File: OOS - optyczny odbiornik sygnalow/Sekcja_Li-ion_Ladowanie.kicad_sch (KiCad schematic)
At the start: 41 parts, among them J1 Conn_01x02_Pin, Q1 SI2301CDS-T1-GE3, Q2 AOSS32334C, Q3 AOSS32334C, U4 MCP73831-2-OT, U5 AP9101CAK6-ANTRG1, U6 AP2126K-ADJTRG1

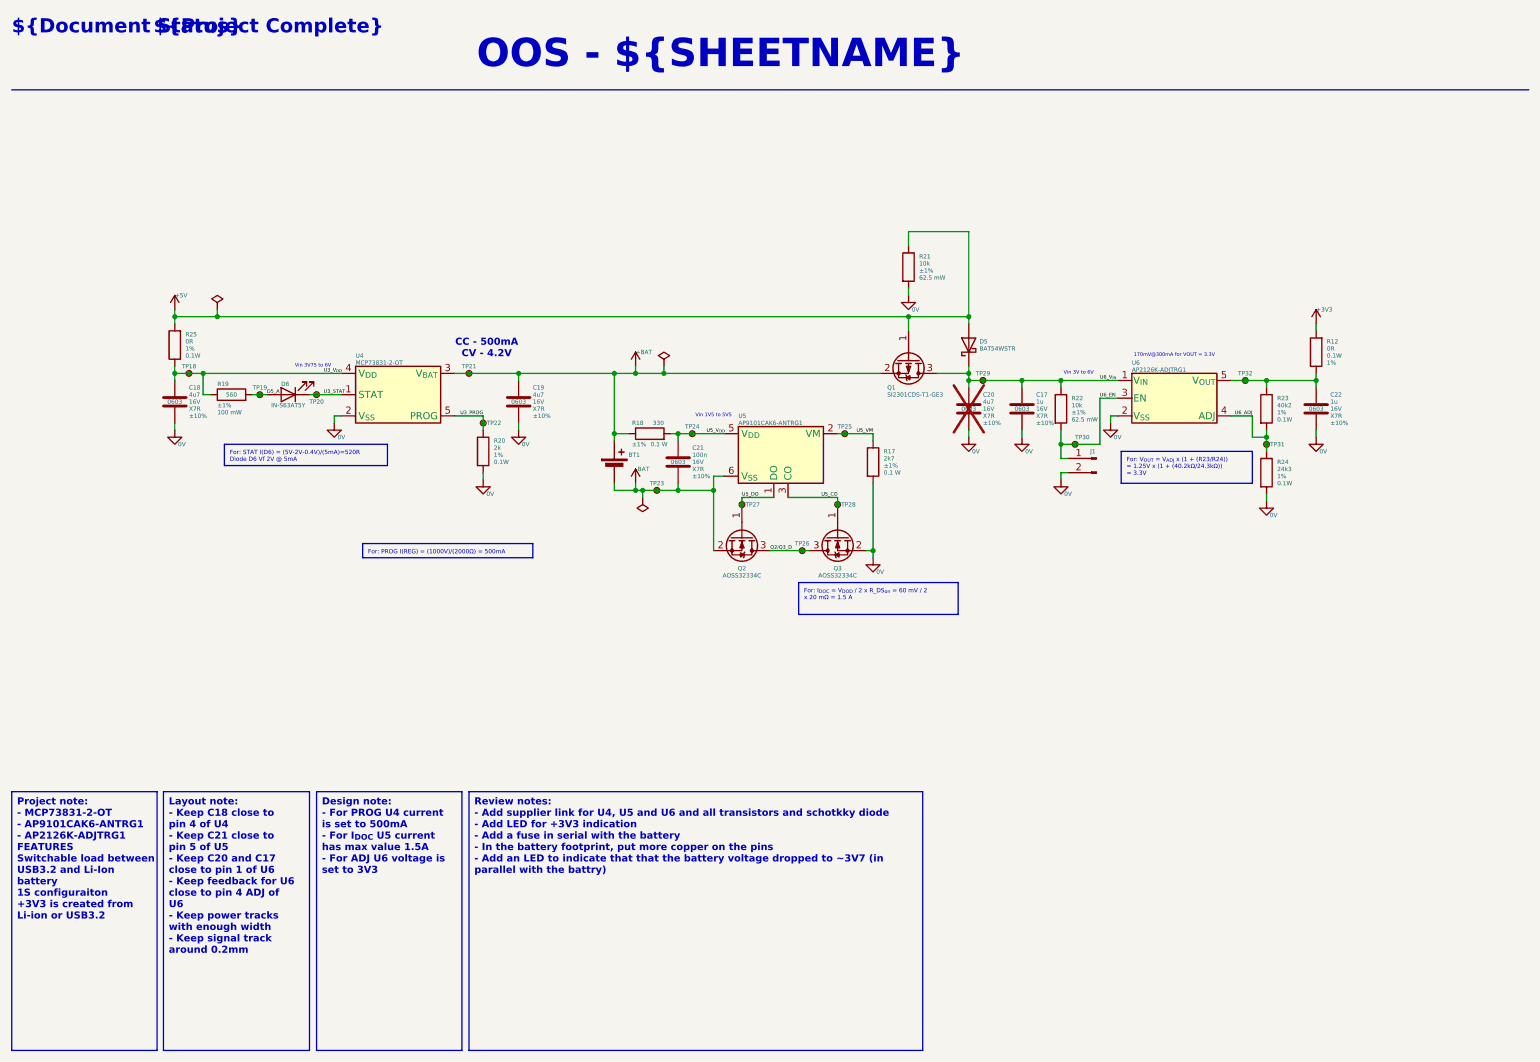
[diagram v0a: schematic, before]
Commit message: Implementing changes after review on Li-Ion section, adding components to USB section
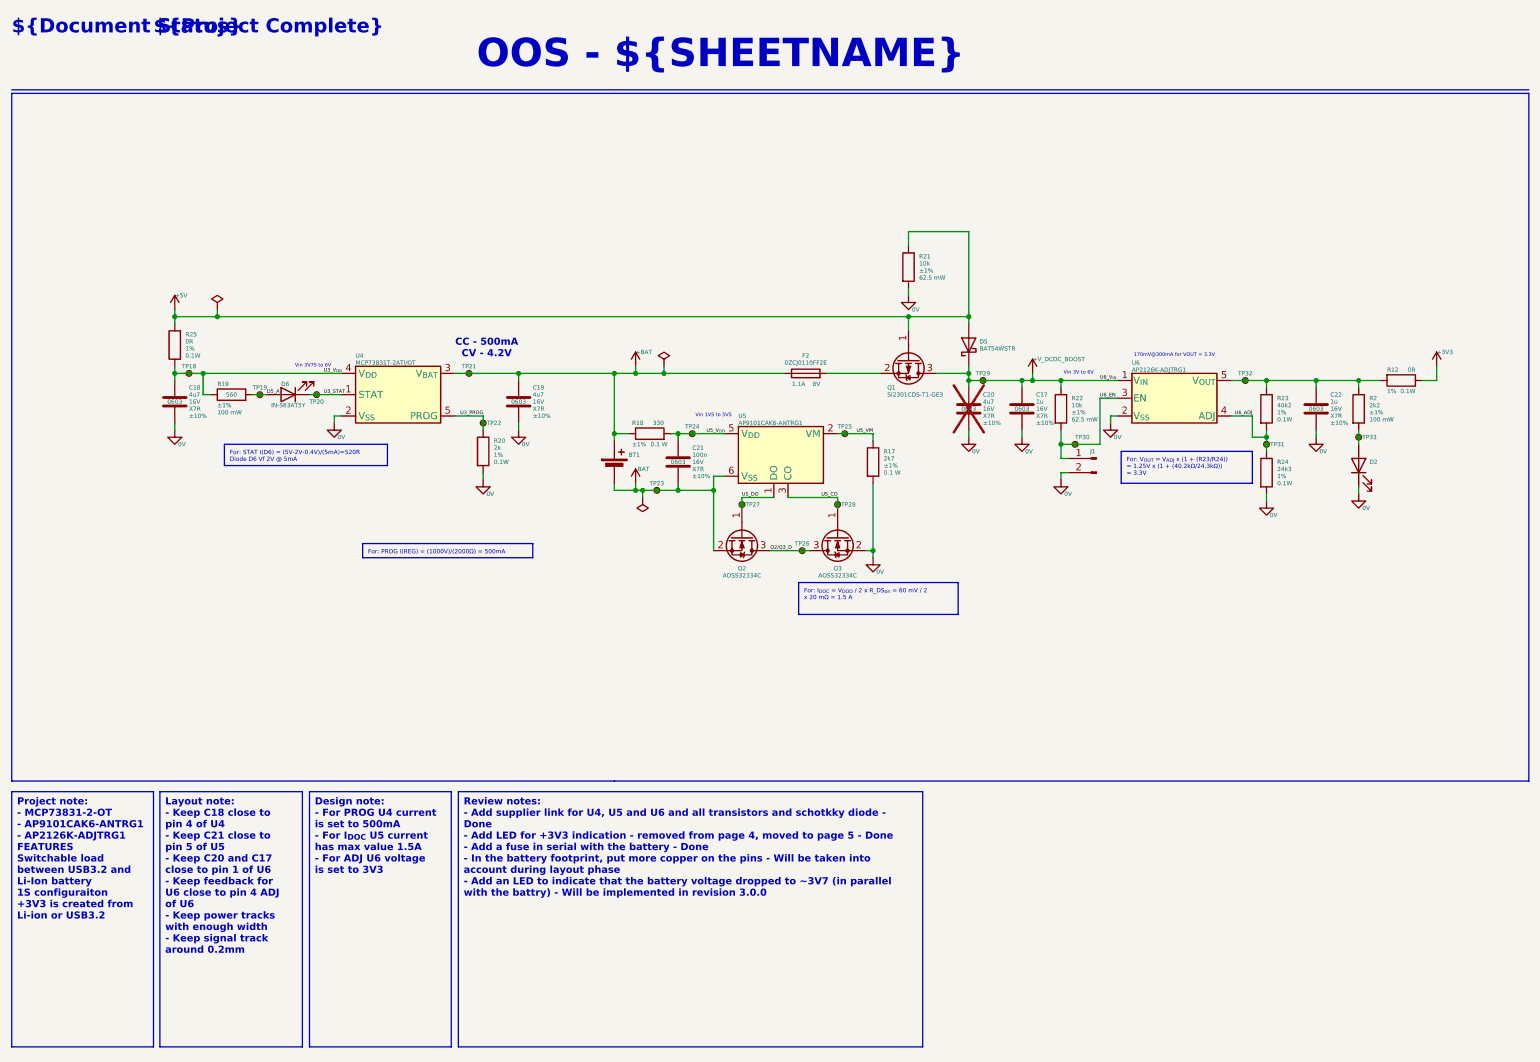
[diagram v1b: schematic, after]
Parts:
- added D2: LED, Diode_SMD:D_0603_1608Metric_Pad1.05x0.95mm_HandSolder, symbol Device:LED
- added F2: 0ZCJ0110FF2E, Fuse:Fuse_1206_3216Metric, symbol Device:Fuse
- added R2: 2k2, Resistor_SMD:R_0603_1608Metric_Pad0.98x0.95mm_HandSolder, symbol Device:R
- added TP33: TestPoint_Small, TestPoint:TestPoint_Pad_D1.0mm, symbol Connector:TestPoint_Small
- U4: value MCP73831-2-OT -> MCP73831T-2ATI/OT; Supplier Link (none) -> https://www.tme.eu/pl/details/mcp73831t-2ati_ot/kontrolery-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
- U5: Supplier Link (none) -> https://www.tme.eu/pl/details/ap9101cak6-antrg1/kontrolery-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
- U6: Supplier Link (none) -> https://www.tme.eu/pl/details/ap2126k-adjtrg1/stabilizatory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
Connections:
- net +3V3: now also R12.1; no longer R12.2
- net +BAT: now also F2.1; no longer Q1.2 (S)
- net 0V: now also D2.1 (K)
- net at C22.1, R23.1, TP32.1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: now also R12.2, R2.1; no longer R12.1
- net U6_V_{IN} renamed +V_DCDC_BOOST
- new net: D2.2 (A), R2.2, TP33.1
- new net: F2.2, Q1.2 (S)
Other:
- moved on the sheet: R12

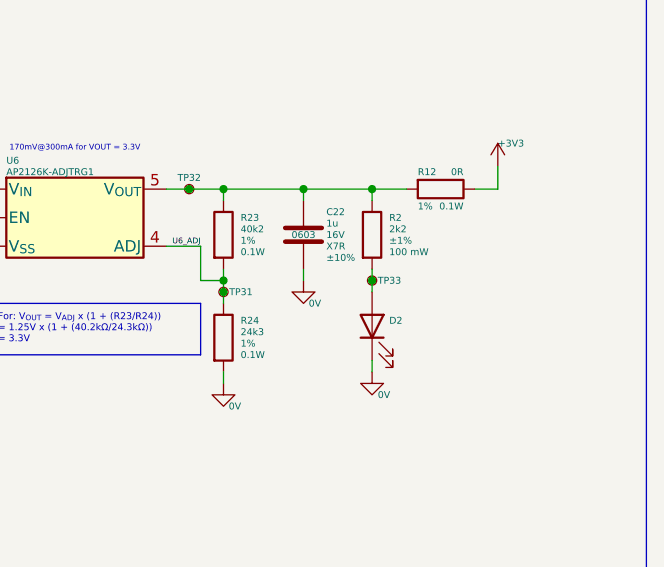
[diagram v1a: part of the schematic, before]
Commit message: trying a different placement for components
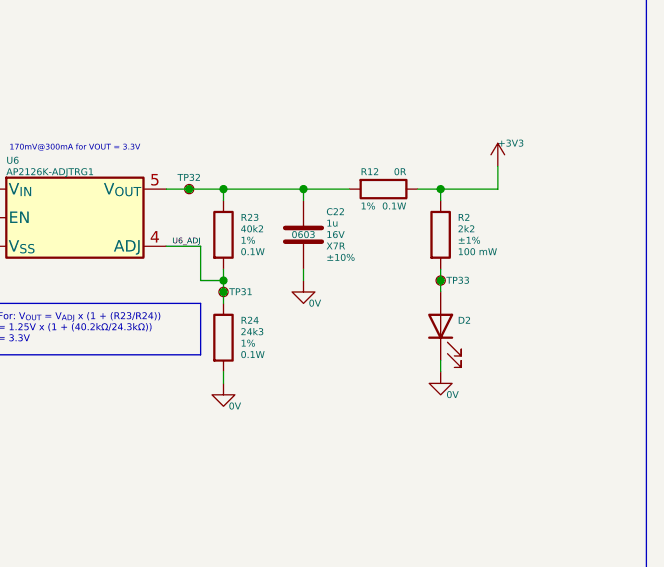
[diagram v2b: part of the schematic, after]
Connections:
- net +3V3: now also R2.1
- net at C22.1, R12.2, R23.1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: no longer R2.1
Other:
- moved on the sheet: D2, R12, R2, TP33
